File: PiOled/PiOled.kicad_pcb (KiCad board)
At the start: 2 copper layers, 65 x 14 mm, 10 parts, among them J1 Raspberry_Pi_2_3, J2 PWR_IN, J3 OLED, J4 GPIO

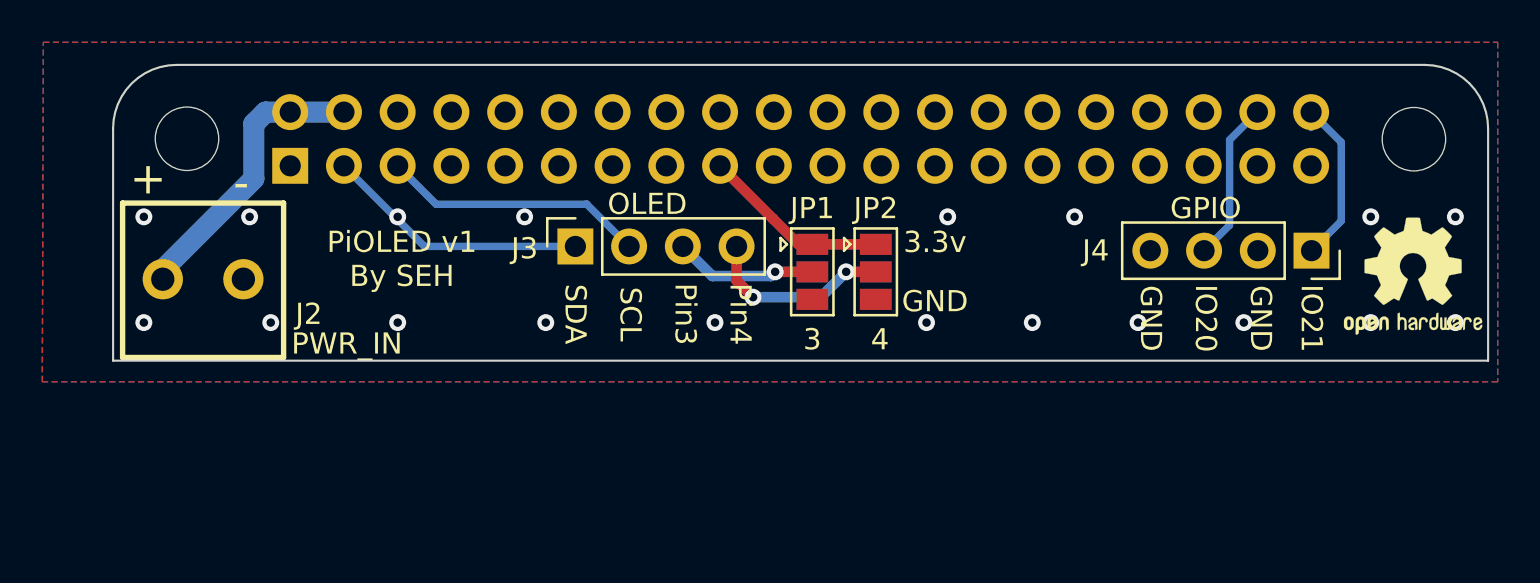
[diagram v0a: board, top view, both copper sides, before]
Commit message: added power distros
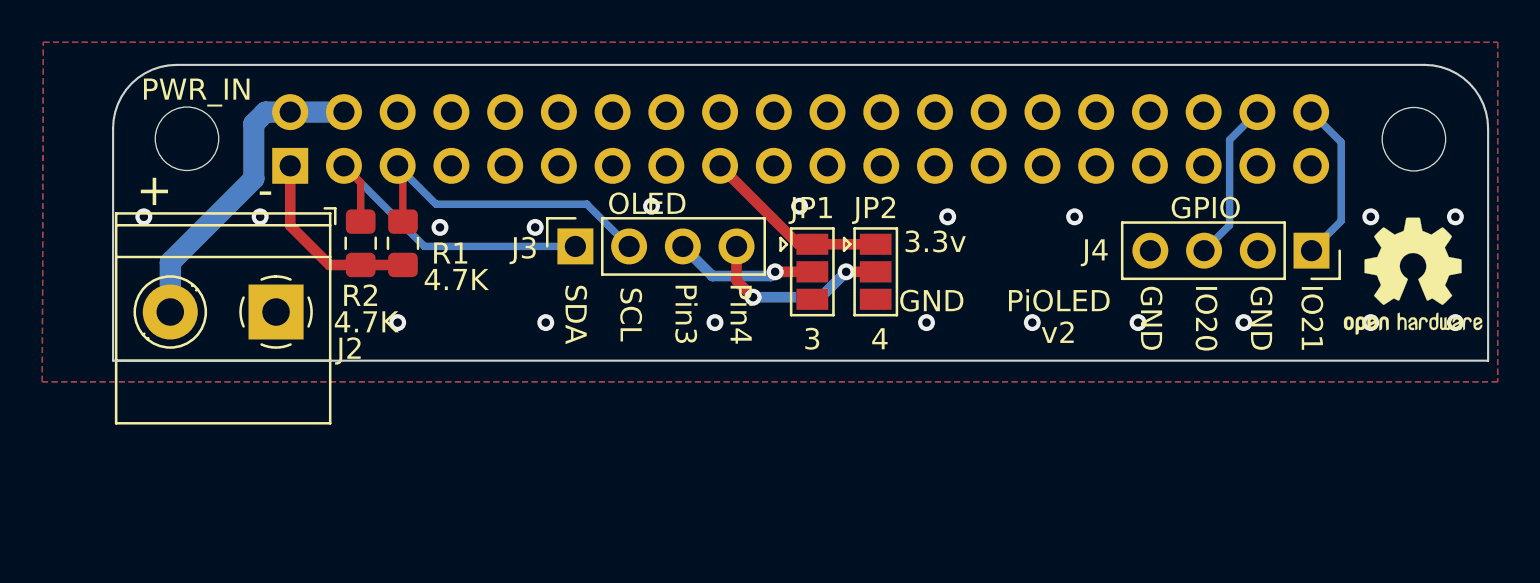
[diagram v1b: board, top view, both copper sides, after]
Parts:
- added R1: 4.7K, Resistor_SMD:R_0805_2012Metric_Pad1.15x1.40mm_HandSolder, F.Cu at (92.2, 69.2)
- added R2: 4.7K, Resistor_SMD:R_0805_2012Metric_Pad1.15x1.40mm_HandSolder, F.Cu at (90.2, 69.2)
- J2: footprint MKDS1_2-3.81:PHOENIX_MKDS1_2-3.81 -> TerminalBlock_Phoenix:TerminalBlock_Phoenix_MKDS-1,5-2_1x02_P5.00mm_Horizontal
- moved J2 3.76 mm to (86.2, 72.5)
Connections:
- J1 pad 1: Net-(J1-Pad1) -> +3.3VP
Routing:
- net +3.3VP: track 0.00 -> 9.02 mm
- net I2C_SDA: track 12.5 -> 15.5 mm, vias 1 -> 0
- net I2C_SCL: track 13.0 -> 15.7 mm
- net +5V: track 13.6 -> 15.0 mm
- net GND: vias 18 -> 19
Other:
- board text added: "PiOLED"
- board text added: "v2"
- board text removed: "PiOLED v1 By SEH"

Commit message: update to add EDM RDS header
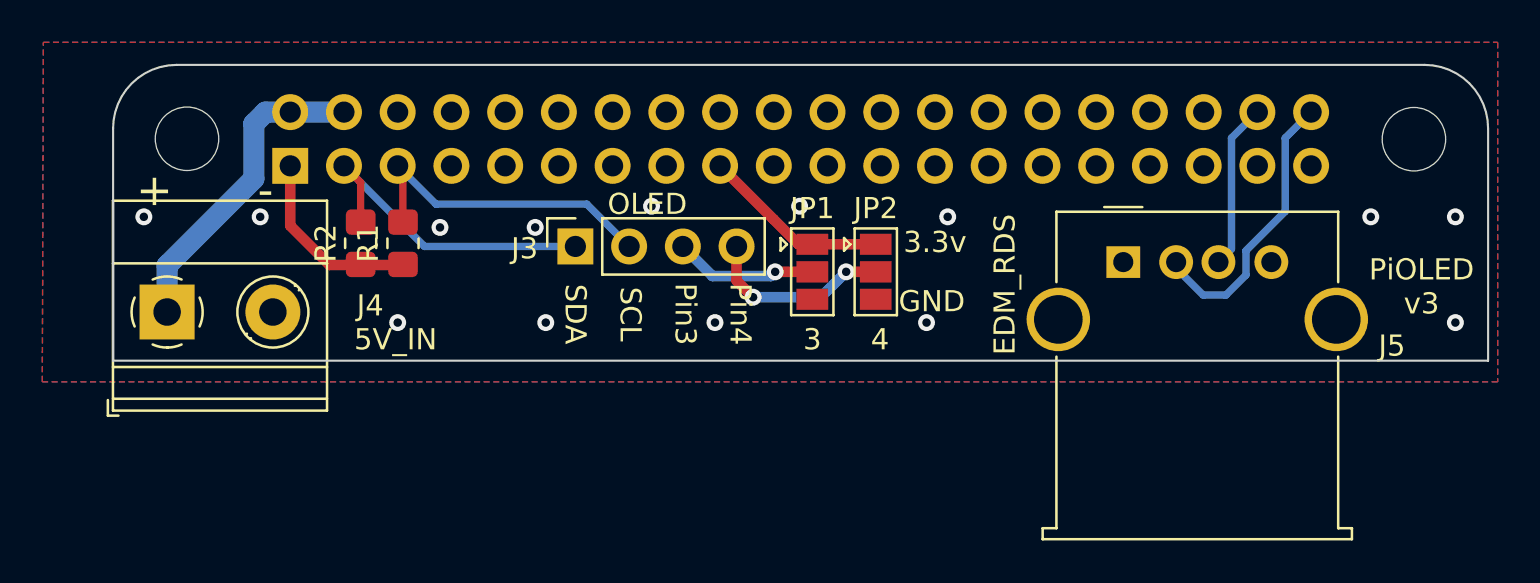
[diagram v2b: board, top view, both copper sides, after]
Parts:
- removed the J4 at (135.2, 69.6)
- removed REF**: OSHW-Logo2_7.3x6mm_SilkScreen, Symbol:OSHW-Logo2_7.3x6mm_SilkScreen
- removed REF**: KiCad-Logo2_5mm_SilkScreen, Symbol:KiCad-Logo2_5mm_SilkScreen
- added J5: EDM_RDS, Connector_USB:USB_A_Molex_67643_Horizontal, F.Cu at (126.3, 70.1)
- J4: renamed from J2; value PWR_IN -> 5V_IN
- R1, R2: footprint Resistor_SMD:R_0805_2012Metric_Pad1.15x1.40mm_HandSolder -> Resistor_SMD:R_0805_2012Metric_Pad1.20x1.40mm_HandSolder
- moved J4 5.15 mm to (81.1, 72.5), turned to 0 degrees
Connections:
- J1 pad 10: Net-(J1-Pad10) -> unconnected-(J1-GPIO15/RXD-Pad10)
- J1 pad 11: Net-(J1-Pad11) -> unconnected-(J1-GPIO17-Pad11)
- J1 pad 12: Net-(J1-Pad12) -> unconnected-(J1-GPIO18/PWM0-Pad12)
- J1 pad 13: Net-(J1-Pad13) -> unconnected-(J1-GPIO27-Pad13)
- J1 pad 15: Net-(J1-Pad15) -> unconnected-(J1-GPIO22-Pad15)
- J1 pad 16: Net-(J1-Pad16) -> unconnected-(J1-GPIO23-Pad16)
- J1 pad 18: Net-(J1-Pad18) -> unconnected-(J1-GPIO24-Pad18)
- J1 pad 19: Net-(J1-Pad19) -> unconnected-(J1-MOSI0/GPIO10-Pad19)
- J1 pad 21: Net-(J1-Pad21) -> unconnected-(J1-MISO0/GPIO9-Pad21)
- J1 pad 22: Net-(J1-Pad22) -> unconnected-(J1-GPIO25-Pad22)
- J1 pad 23: Net-(J1-Pad23) -> unconnected-(J1-SCLK0/GPIO11-Pad23)
- J1 pad 24: Net-(J1-Pad24) -> unconnected-(J1-~{CE0}/GPIO8-Pad24)
- J1 pad 26: Net-(J1-Pad26) -> unconnected-(J1-~{CE1}/GPIO7-Pad26)
- J1 pad 27: Net-(J1-Pad27) -> unconnected-(J1-ID_SD/GPIO0-Pad27)
- J1 pad 28: Net-(J1-Pad28) -> unconnected-(J1-ID_SC/GPIO1-Pad28)
- J1 pad 29: Net-(J1-Pad29) -> unconnected-(J1-GCLK1/GPIO5-Pad29)
- J1 pad 31: Net-(J1-Pad31) -> unconnected-(J1-GCLK2/GPIO6-Pad31)
- J1 pad 32: Net-(J1-Pad32) -> unconnected-(J1-PWM0/GPIO12-Pad32)
- J1 pad 33: Net-(J1-Pad33) -> unconnected-(J1-PWM1/GPIO13-Pad33)
- J1 pad 35: Net-(J1-Pad35) -> unconnected-(J1-GPIO19/MISO1-Pad35)
- J1 pad 36: Net-(J1-Pad36) -> unconnected-(J1-GPIO16-Pad36)
- J1 pad 37: Net-(J1-Pad37) -> unconnected-(J1-GPIO26-Pad37)
- J1 pad 7: Net-(J1-Pad7) -> unconnected-(J1-GCLK0/GPIO4-Pad7)
- J1 pad 8: Net-(J1-Pad8) -> unconnected-(J1-GPIO14/TXD-Pad8)
- J4 pad 1: GND -> +5V
- J4 pad 2: +5V -> GND
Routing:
- net GPIO21: track 8.45 -> 13.5 mm
- net GND: vias 19 -> 14
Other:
- net class 3.3V removed
- net class 5V removed
- net class Default removed
- net class PWR removed
- board text added: "${TITLE} ${REVISION}"
- board text removed: "IO20"
- board text removed: "IO21"
- board text removed: "PiOLED"
- board text removed: "v2"

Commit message: add plug in 3 to 4 adapter
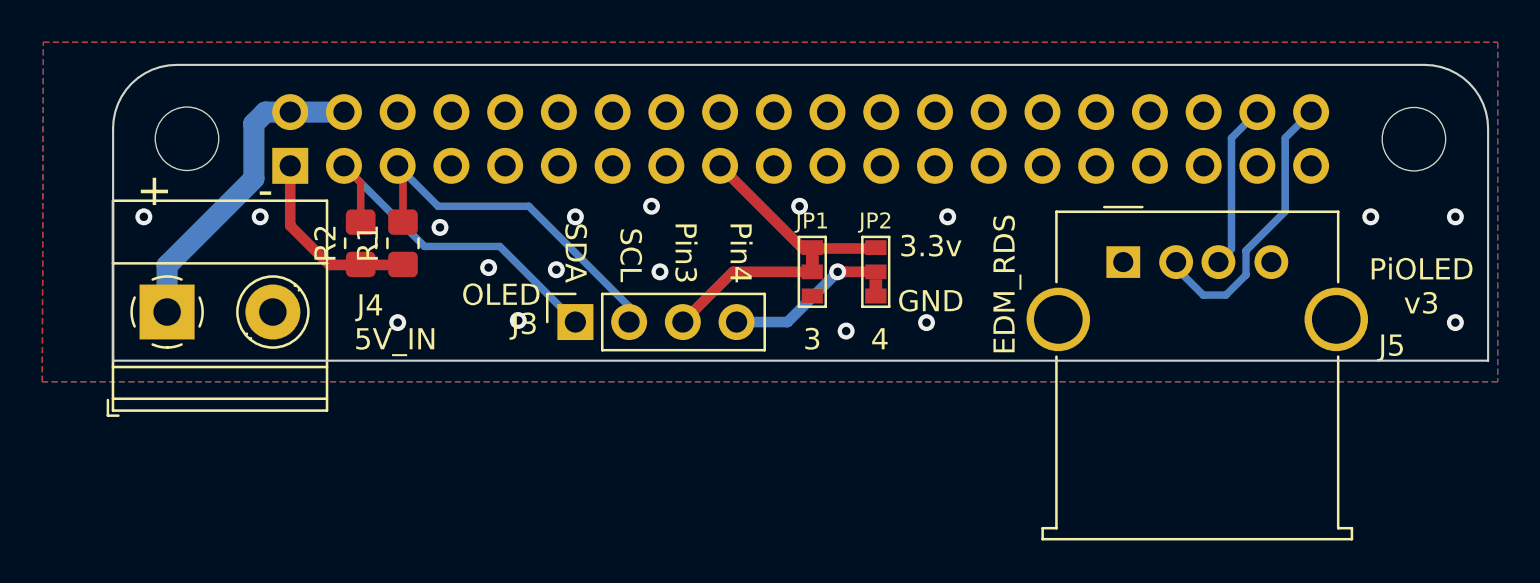
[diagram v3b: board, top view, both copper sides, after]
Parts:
- JP1: footprint Jumper:SolderJumper-3_P1.3mm_Open_Pad1.0x1.5mm -> Scotts:SolderJumper-3_P1mm_Bridged12
- JP2: footprint Jumper:SolderJumper-3_P1.3mm_Open_Pad1.0x1.5mm -> Scotts:SolderJumper-3_P1mm_Bridged23
- moved J3 3.57 mm to (100.4, 73.0)
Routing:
- net I2C_SCL: track 15.7 -> 17.6 mm
- net I2C_SDA: track 15.5 -> 17.0 mm
- net /PIN4: track 9.02 -> 7.56 mm, vias 2 -> 1
- net /PIN3: track 6.78 -> 7.10 mm, vias 1 -> 0
- net GND: vias 14 -> 17
